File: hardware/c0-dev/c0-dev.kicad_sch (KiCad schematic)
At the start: 17 parts, among them J1 2913730000, J10 2913730000, J11 2913730000, J12 2913710000, J13 2913730000, J14 2913730000, J2 2913710000, J3 2913730000, J4 2913730000, J5 2913710000, J6 2913730000, J7 2913730000, J8 2913710000, J9 2913730000

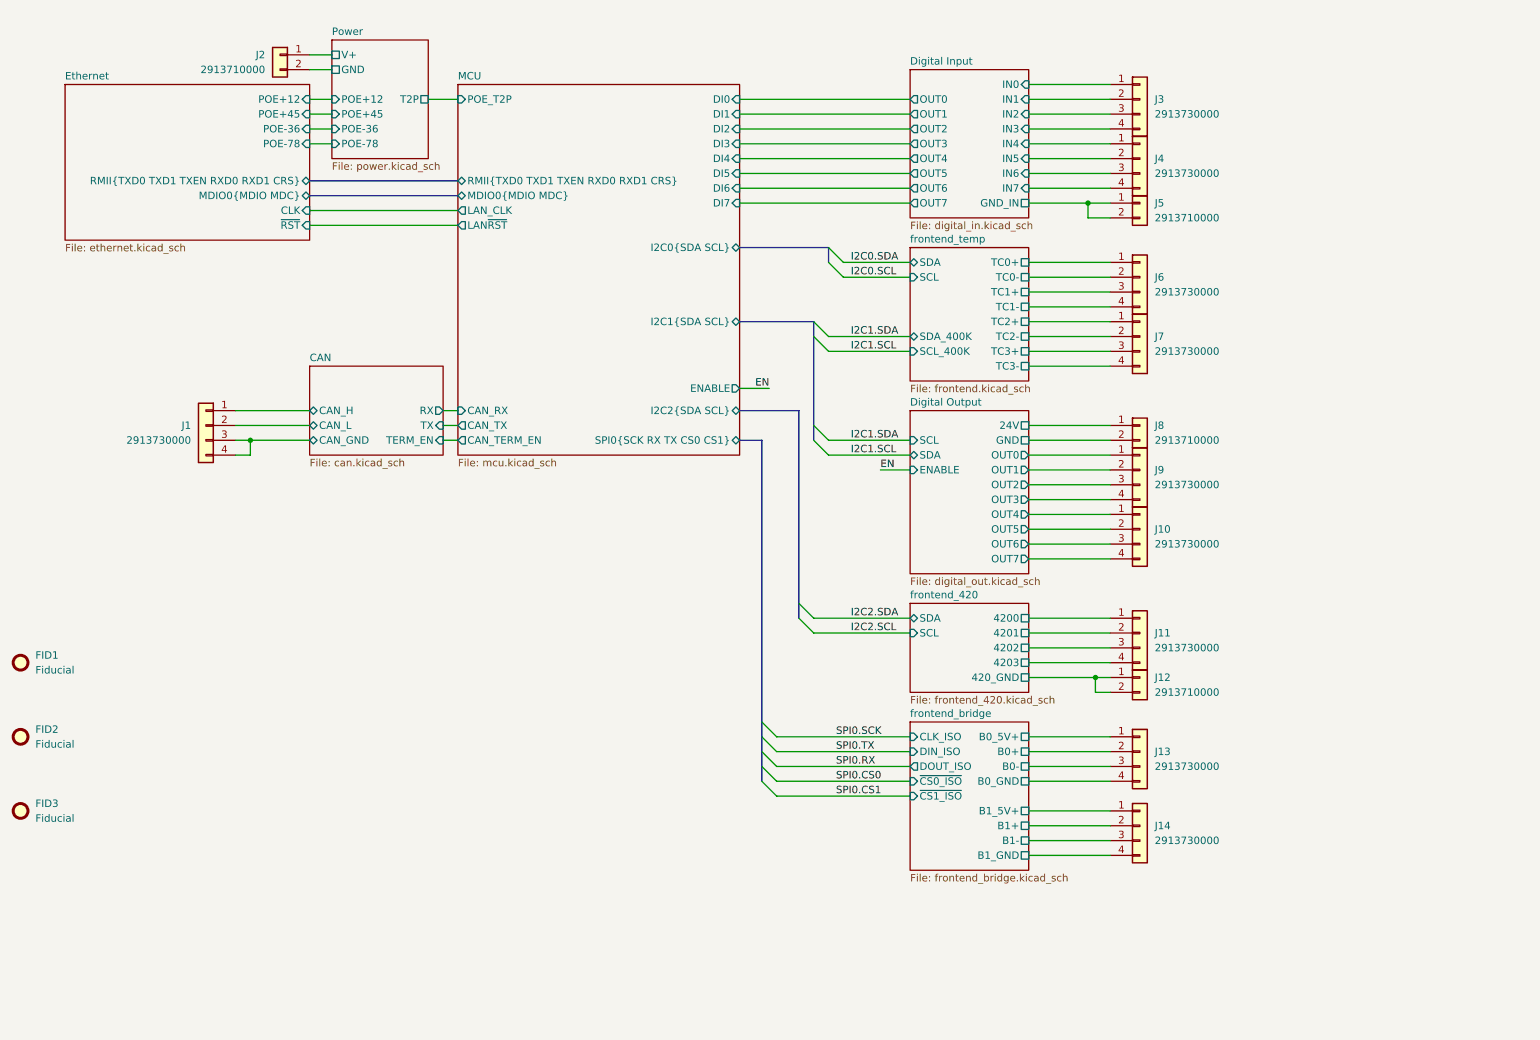
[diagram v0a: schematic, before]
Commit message: page based annotation + flybuck fb
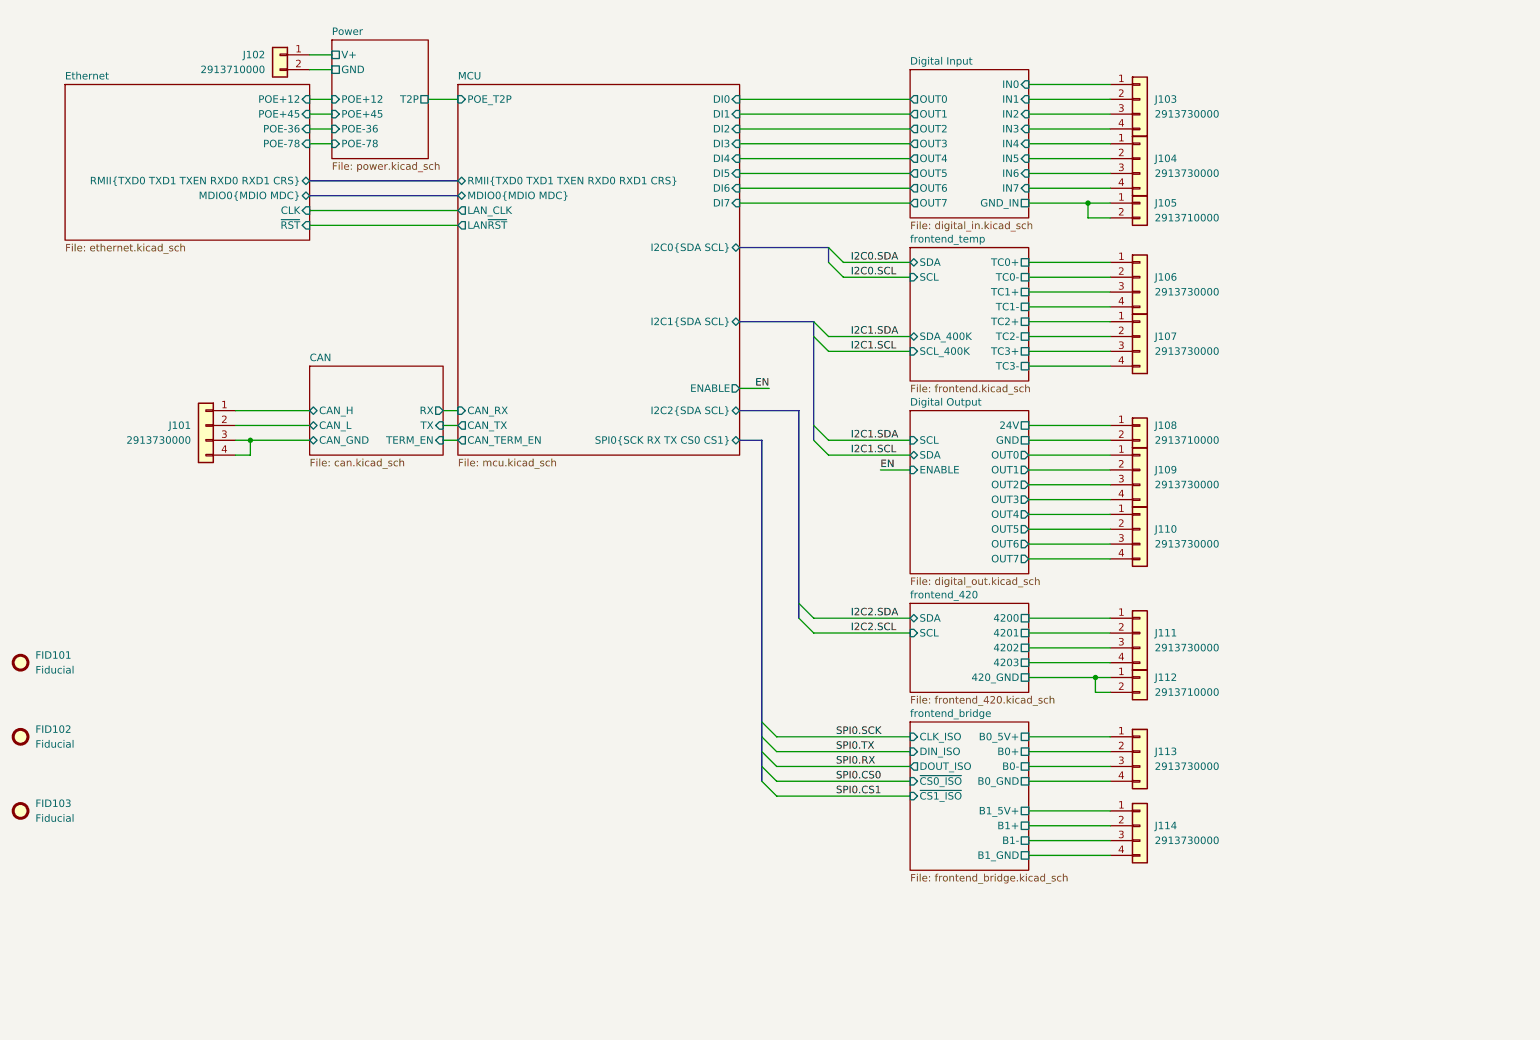
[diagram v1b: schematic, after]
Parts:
- renumbered FID1 to FID101, FID2 to FID102, FID3 to FID103, J1 to J101, J2 to J102, J3 to J103, J4 to J104, J5 to J105, J6 to J106, J7 to J107, J8 to J108, J9 to J109, J10 to J110, J11 to J111, J12 to J112, J13 to J113, J14 to J114
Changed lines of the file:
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@@
 		(in_pos_files yes)
 		(dnp no)
-		(property "Reference" "J2"
+		(property "Reference" "J102"
 			(at 67.31 22.8599 0)
 			(show_name no)
@@
 			(project "c0-dev"
 				(path "/b8347a0e-ad04-4414-969d-3c64a611d74e"
-					(reference "J2")
+					(reference "J102")
 					(unit 1)
 				)
@@
 		(dnp no)
 		(fields_autoplaced yes)
-		(property "Reference" "J8"
+		(property "Reference" "J108"
 			(at 219.71 86.3599 0)
 			(show_name no)
@@
 			(project "c0-dev"
 				(path "/b8347a0e-ad04-4414-969d-3c64a611d74e"
-					(reference "J8")
+					(reference "J108")
 					(unit 1)
 				)
@@
 		(dnp no)
 		(fields_autoplaced yes)
-		(property "Reference" "J12"
+		(property "Reference" "J112"
 			(at 219.71 129.5399 0)
 			(show_name no)
@@
 			(project "c0-dev"
 				(path "/b8347a0e-ad04-4414-969d-3c64a611d74e"
-					(reference "J12")
+					(reference "J112")
 					(unit 1)
 				)
@@
 		(dnp no)
 		(fields_autoplaced yes)
-		(property "Reference" "J14"
+		(property "Reference" "J114"
 			(at 219.71 154.9399 0)
 			(show_name no)
@@
 			(project "c0-dev"
 				(path "/b8347a0e-ad04-4414-969d-3c64a611d74e"
-					(reference "J14")
+					(reference "J114")
 					(unit 1)
 				)
@@
 		(dnp no)
 		(fields_autoplaced yes)
-		(property "Reference" "J13"
+		(property "Reference" "J113"
 			(at 219.71 142.2399 0)
 			(show_name no)
@@
 			(project "c0-dev"
 				(path "/b8347a0e-ad04-4414-969d-3c64a611d74e"
-					(reference "J13")
+					(reference "J113")
 					(unit 1)
 				)
@@
 		(dnp no)
 		(fields_autoplaced yes)
-		(property "Reference" "J11"
+		(property "Reference" "J111"
 			(at 219.71 121.9199 0)
 			(show_name no)
@@
 			(project "c0-dev"
 				(path "/b8347a0e-ad04-4414-969d-3c64a611d74e"
-					(reference "J11")
+					(reference "J111")
 					(unit 1)
 				)
@@
 		(dnp no)
 		(fields_autoplaced yes)
-		(property "Reference" "J6"
+		(property "Reference" "J106"
 			(at 219.71 60.9599 0)
 			(show_name no)
@@
 			(project "c0-dev"
 				(path "/b8347a0e-ad04-4414-969d-3c64a611d74e"
-					(reference "J6")
+					(reference "J106")
 					(unit 1)
 				)
@@
 		(dnp no)
 		(fields_autoplaced yes)
-		(property "Reference" "FID1"
+		(property "Reference" "FID101"
 			(at 27.94 125.7299 0)
 			(show_name no)
@@
 			(project "c0-dev"
 				(path "/b8347a0e-ad04-4414-969d-3c64a611d74e"
-					(reference "FID1")
+					(reference "FID101")
 					(unit 1)
 				)
@@
 		(dnp no)
 		(fields_autoplaced yes)
-		(property "Reference" "J3"
+		(property "Reference" "J103"
 			(at 219.71 30.4799 0)
 			(show_name no)
@@
 			(project "c0-dev"
 				(path "/b8347a0e-ad04-4414-969d-3c64a611d74e"
-					(reference "J3")
+					(reference "J103")
 					(unit 1)
 				)
@@
 		(in_pos_files yes)
 		(dnp no)
-		(property "Reference" "J1"
+		(property "Reference" "J101"
 			(at 54.61 86.3599 0)
 			(show_name no)
@@
 			(project "c0-dev"
 				(path "/b8347a0e-ad04-4414-969d-3c64a611d74e"
-					(reference "J1")
+					(reference "J101")
 					(unit 1)
 				)
@@
 		(dnp no)
 		(fields_autoplaced yes)
-		(property "Reference" "J5"
+		(property "Reference" "J105"
 			(at 219.71 48.2599 0)
 			(show_name no)
@@
 			(project "c0-dev"
 				(path "/b8347a0e-ad04-4414-969d-3c64a611d74e"
-					(reference "J5")
+					(reference "J105")
 					(unit 1)
 				)
@@
 		(dnp no)
 		(fields_autoplaced yes)
-		(property "Reference" "J9"
+		(property "Reference" "J109"
 			(at 219.71 93.9799 0)
 			(show_name no)
@@
 			(project "c0-dev"
 				(path "/b8347a0e-ad04-4414-969d-3c64a611d74e"
-					(reference "J9")
+					(reference "J109")
 					(unit 1)
 				)
@@
 		(dnp no)
 		(fields_autoplaced yes)
-		(property "Reference" "FID2"
+		(property "Reference" "FID102"
 			(at 27.94 138.4299 0)
 			(show_name no)
@@
 			(project "c0-dev"
 				(path "/b8347a0e-ad04-4414-969d-3c64a611d74e"
-					(reference "FID2")
+					(reference "FID102")
 					(unit 1)
 				)
@@
 		(dnp no)
 		(fields_autoplaced yes)
-		(property "Reference" "J7"
+		(property "Reference" "J107"
 			(at 219.71 71.1199 0)
 			(show_name no)
@@
 			(project "c0-dev"
 				(path "/b8347a0e-ad04-4414-969d-3c64a611d74e"
-					(reference "J7")
+					(reference "J107")
 					(unit 1)
 				)
@@
 		(dnp no)
 		(fields_autoplaced yes)
-		(property "Reference" "FID3"
+		(property "Reference" "FID103"
 			(at 27.94 151.1299 0)
 			(show_name no)
@@
 			(project "c0-dev"
 				(path "/b8347a0e-ad04-4414-969d-3c64a611d74e"
-					(reference "FID3")
+					(reference "FID103")
 					(unit 1)
 				)
@@
 		(dnp no)
 		(fields_autoplaced yes)
-		(property "Reference" "J10"
+		(property "Reference" "J110"
 			(at 219.71 104.1399 0)
 			(show_name no)
@@
 			(project "c0-dev"
 				(path "/b8347a0e-ad04-4414-969d-3c64a611d74e"
-					(reference "J10")
+					(reference "J110")
 					(unit 1)
 				)
@@
 		(dnp no)
 		(fields_autoplaced yes)
-		(property "Reference" "J4"
+		(property "Reference" "J104"
 			(at 219.71 40.6399 0)
 			(show_name no)
@@
 			(project "c0-dev"
 				(path "/b8347a0e-ad04-4414-969d-3c64a611d74e"
-					(reference "J4")
-					(unit 1)
-				)
+					(reference "J104")
+					(unit 1)
+				)

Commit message: power and isolation cleanup
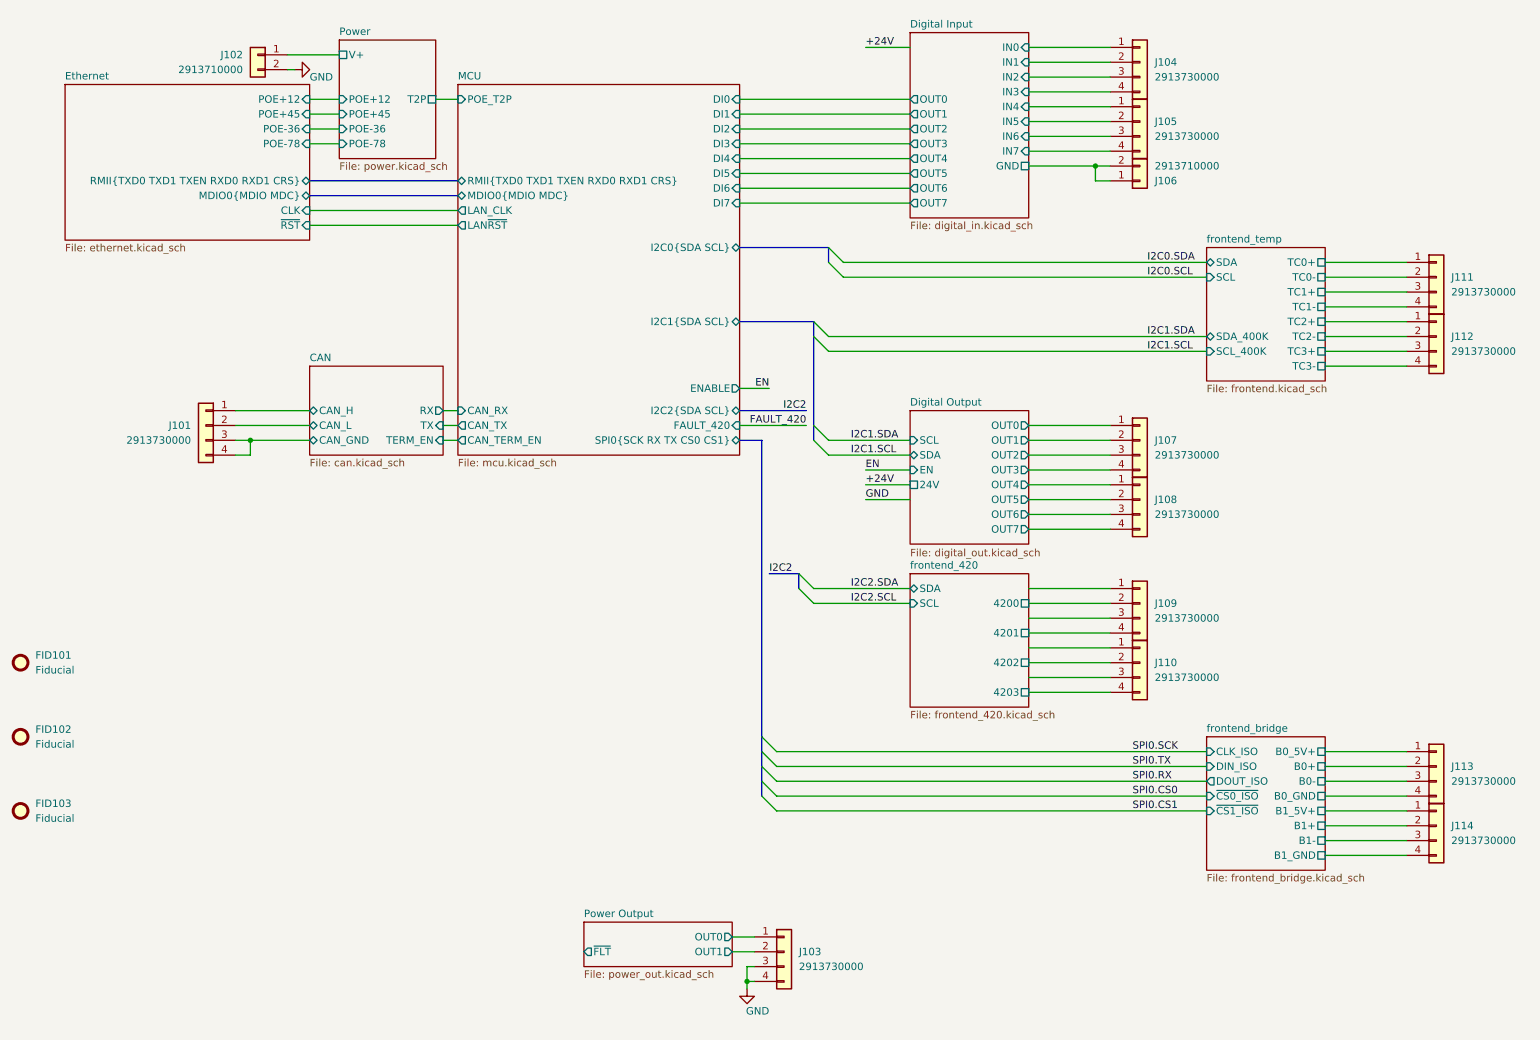
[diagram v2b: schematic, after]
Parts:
- removed J105, J108, J112: 2913710000, conduit:2913710000, symbol Connector_Generic:Conn_01x02
- added J103, J110: 2913730000, conduit:2913730000, symbol Connector_Generic:Conn_01x04
- added J106: 2913710000, conduit:2913710000, symbol Connector_Generic:Conn_01x02
- renumbered J103 to J104, J104 to J105, J109 to J107, J110 to J108, J111 to J109, J106 to J111, J107 to J112
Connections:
- net frontend_420/4200: now also J109.2 (Pin_2); no longer J109.1 (Pin_1)
- net frontend_420/4201: now also J109.4 (Pin_4); no longer J109.2 (Pin_2)
- net frontend_420/4202: now also J110.2 (Pin_2); no longer J109.3 (Pin_3)
- net frontend_420/4203: now also J110.4 (Pin_4); no longer J109.4 (Pin_4)
- net Power/GND renamed GND
- net GND: now also J103.3 (Pin_3), J103.4 (Pin_4)
- new net Digital Input/GND: J106.1 (Pin_1), J106.2 (Pin_2)
- new net Power Output/OUT0: J103.1 (Pin_1)
- new net Power Output/OUT1: J103.2 (Pin_2)
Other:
- added sheet Power Output (power_out.kicad_sch)
- sheet Digital Input ports: added GND; removed GND_IN
- sheet Digital Output ports: added EN; removed ENABLE, GND
- sheet MCU ports: added FAULT_420; removed none
- sheet Power ports: added none; removed GND
- sheet frontend_420 ports: added none; removed 420_GND
- moved on the sheet: J102, J104, J105, J107, J108, J109, J111, J112, J113, J114

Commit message: cjc overhaul
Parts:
- removed J110: 2913730000, conduit:2913730000, symbol Connector_Generic:Conn_01x04
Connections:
- net frontend_420/4200: now also J109.1 (Pin_1); no longer J109.2 (Pin_2)
- net frontend_420/4201: now also J109.2 (Pin_2); no longer J109.4 (Pin_4)
- net frontend_420/4202: now also J109.3 (Pin_3)
- net frontend_420/4203: now also J109.4 (Pin_4)
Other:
- sheet frontend_temp: file frontend.kicad_sch -> frontend_tc.kicad_sch
- moved on the sheet: J113, J114
